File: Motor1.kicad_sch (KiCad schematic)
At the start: 53 parts, among them J601 Step Out, J604 Direction, J605 Direction, Q601 WSF07N10, Q602 WSF07N10, Q603 WSF07N10, Q604 WSF07N10, Q605 WSF07N10, Q606 WSF07N10, Q607 WSF07N10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

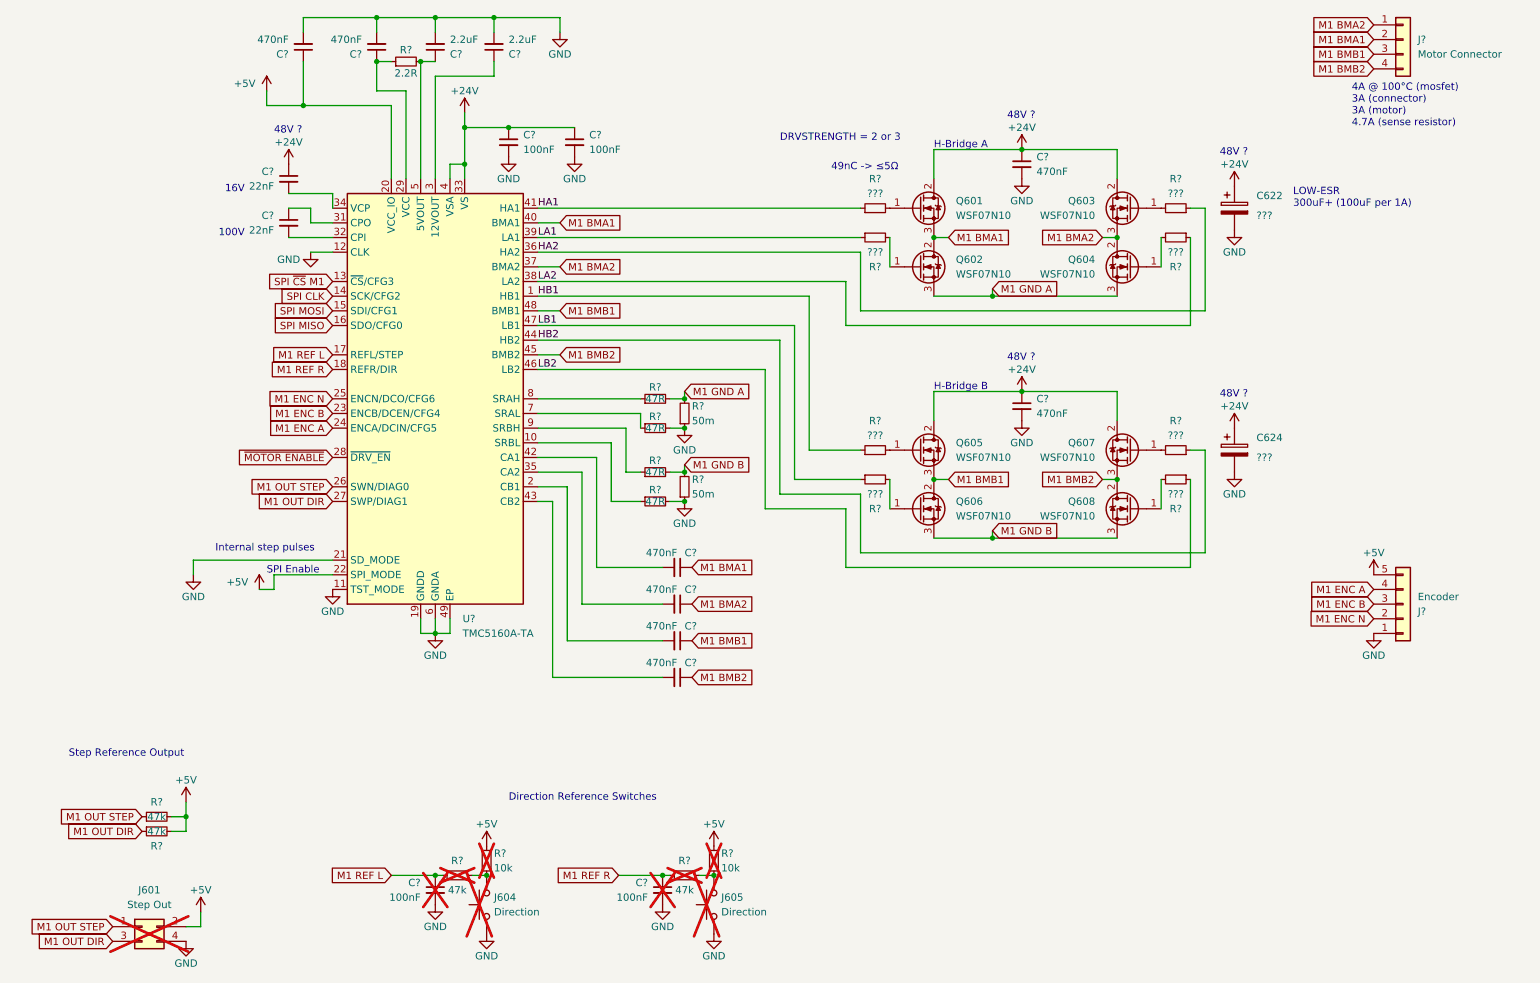
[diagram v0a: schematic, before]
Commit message: Complete schematics Assign every value (very few exceptions) Change TCM5160 from on-board to separate module Add fuses Add power supplies (LDO + 2x buck converter)
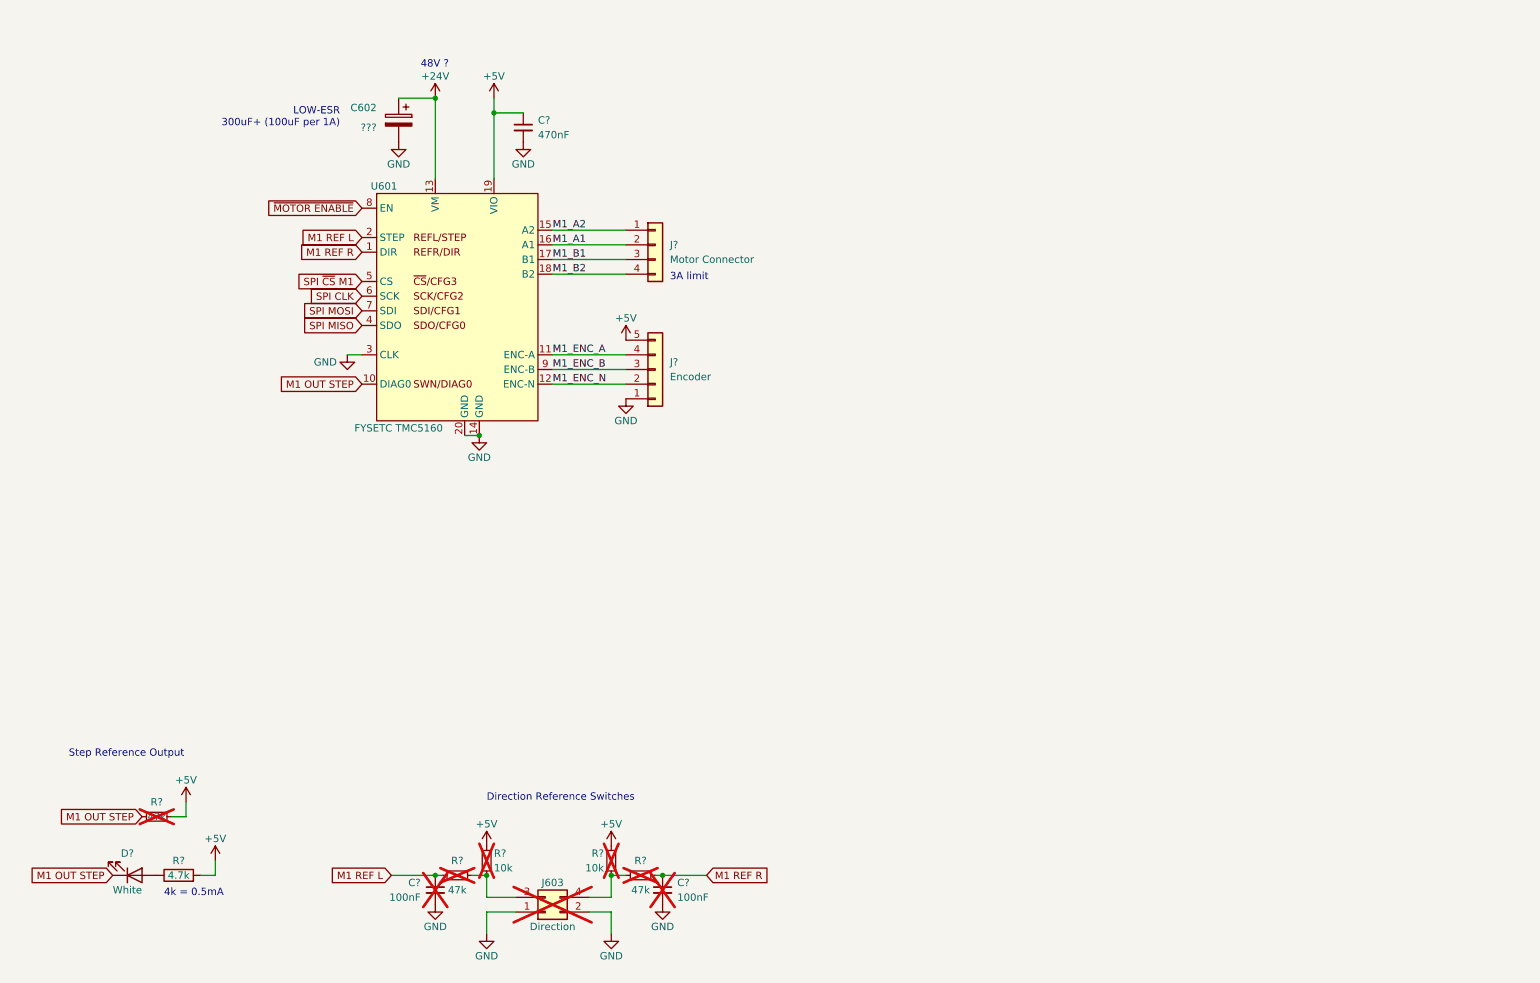
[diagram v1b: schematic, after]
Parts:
- removed C622, C624: ???, symbol Device:C_Polarized
- removed C? (x6): 470nF, Capacitor_SMD:C_1210_3225Metric, symbol Device:C_Small
- removed C? (x4): 100nF, symbol Device:C_Small
- removed C? (x2): 2.2uF, symbol Device:C_Small
- removed C? (x2): 470nF, symbol Device:C_Small
- removed C? (x2): 22nF, symbol Device:C_Small
- removed J601: Step Out, Connector_PinHeader_2.54mm:PinHeader_2x02_P2.54mm_Vertical, symbol Connector_Generic:Conn_02x02_Odd_Even
- removed J604, J605: Direction, Connector_PinHeader_2.54mm:PinHeader_1x02_P2.54mm_Vertical, symbol Switch:SW_Push
- removed J?: Encoder, Connector_JST:JST_XH_B5B-XH-A_1x05_P2.50mm_Vertical, symbol Connector_Generic:Conn_01x05
- removed J?: Motor Connector, Connector_JST:JST_XH_B4B-XH-A_1x04_P2.50mm_Vertical, symbol Connector_Generic:Conn_01x04
- removed Q601, Q602, Q603, Q604, Q605, Q606, Q607, Q608: WSF07N10, Package_TO_SOT_SMD:TO-252-2, symbol Transistor_FET:QM6006D
- removed R? (x2): 50m, Resistor_SMD:R_2512_6332Metric, symbol Device:R_Small
- removed R? (x4): 47k, symbol Device:R_Small
- removed R? (x8): ???, symbol Device:R_Small
- removed R? (x4): 47R, symbol Device:R_Small
- removed R?: 2.2R, symbol Device:R_Small
- removed R? (x2): 10k, symbol Device:R_Small
- removed U?: TMC5160A-TA, Package_QFP:TQFP-48-1EP_7x7mm_P0.5mm_EP5x5mm_ThermalVias, symbol Driver_Motor:TMC5160A-TA
- added C602: ???, symbol Device:C_Polarized
- added C? (x2): 100nF, Capacitor_SMD:C_0402_1005Metric, symbol Device:C_Small
- added C?: 470nF, Capacitor_SMD:C_0603_1608Metric, symbol Device:C_Small
- added D?: White, LED_SMD:LED_0402_1005Metric, symbol Device:LED
- added J603: Direction, Connector_PinHeader_2.54mm:PinHeader_2x02_P2.54mm_Vertical, symbol Connector_Generic:Conn_02x02_Odd_Even
- added J?: Motor Connector, Connector_JST:JST_XH_B4B-XH-A_1x04_P2.50mm_Vertical, symbol Connector_Generic:Conn_01x04
- added J?: Encoder, Connector_JST:JST_XH_B5B-XH-A_1x05_P2.50mm_Vertical, symbol Connector_Generic:Conn_01x05
- added R? (x3): 47k, Resistor_SMD:R_0603_1608Metric, symbol Device:R_Small
- added R? (x2): 10k, Resistor_SMD:R_0603_1608Metric, symbol Device:R_Small
- added R?: 4.7k, Resistor_SMD:R_0603_1608Metric, symbol Device:R
- added U601: FYSETC TMC5160, Custom:FYSETC TMC5160, symbol Custom:FYSETC_TMC5160
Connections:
- net +24V: now also C602.1, U601.13 (VM)
- net +5V: now also C?.1, J?.5 (Pin_5), R?.2, R?.2, R?.2, R?.2, U601.19 (VIO)
- net GND: now also C602.2, C?.2, C?.2, C?.2, J603.1 (Pin_1), J603.2 (Pin_2), J?.1 (Pin_1), U601.14 (GND), U601.20 (GND), U601.3 (CLK)
- net M1 OUT STEP: now also D?.1 (K), R?.1, U601.10 (DIAG0)
- net M1 REF L: now also C?.1, R?.1, U601.2 (STEP)
- net M1 REF R: now also C?.1, R?.1, U601.1 (DIR)
- net SPI CLK: now also U601.6 (SCK)
- net SPI MISO: now also U601.4 (SDO)
- net SPI MOSI: now also U601.7 (SDI)
- net SPI ~{CS} M1: now also U601.5 (CS)
- net ~{MOTOR ENABLE}: now also U601.8 (EN)
- new net: J603.3 (Pin_3), R?.1, R?.2
- new net: J603.4 (Pin_4), R?.1, R?.2
- new net: D?.2 (A), R?.1
- new net M1_A1: J?.2 (Pin_2), U601.16 (A1)
- new net M1_A2: J?.1 (Pin_1), U601.15 (A2)
- new net M1_B1: J?.3 (Pin_3), U601.17 (B1)
- new net M1_B2: J?.4 (Pin_4), U601.18 (B2)
- new net M1_ENC_A: J?.4 (Pin_4), U601.11 (ENC-A)
- new net M1_ENC_B: J?.3 (Pin_3), U601.9 (ENC-B)
- new net M1_ENC_N: J?.2 (Pin_2), U601.12 (ENC-N)
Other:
- note added: "3A limit"
- note added: "4k = 0.5mA"
- note removed: "100V"
- note removed: "16V"
- note removed: "49nC -> ≤5Ω"
- note removed: "4A @ 100°C (mosfet) 3A (connector) 3A (motor) 4.7A (sense resistor)"
- note removed: "DRVSTRENGTH = 2 or 3"
- note removed: "H-Bridge A"
- note removed: "H-Bridge B"
- note removed: "Internal step pulses"
- note removed: "SPI Enable"

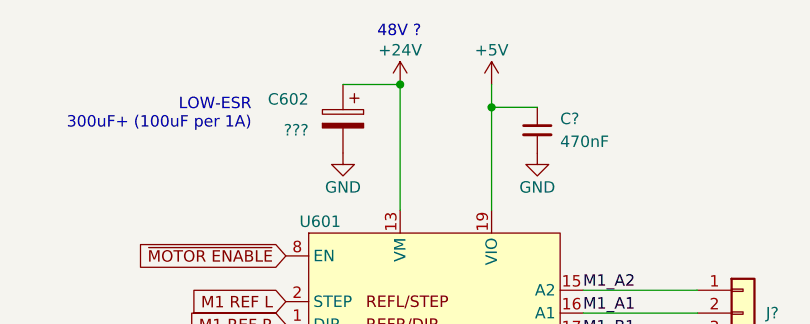
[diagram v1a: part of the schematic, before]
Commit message: More PCB placement, fix 48V for Motors
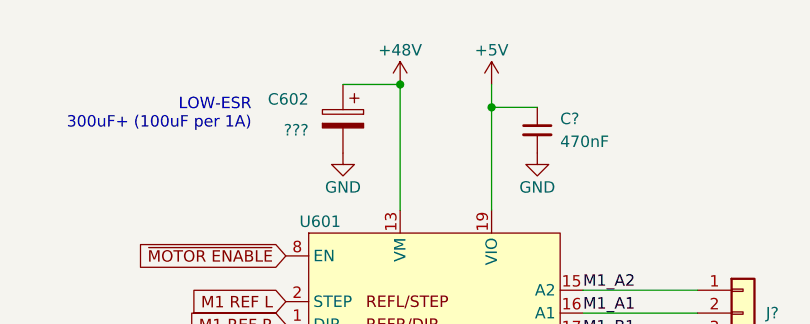
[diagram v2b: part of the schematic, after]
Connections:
- net +24V renamed +48V
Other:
- note removed: "48V ?"
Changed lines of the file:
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@@
   (junction (at 121.92 173.99) (diameter 0) (color 0 0 0 0)
   )
+  (junction (at 91.44 39.37) (diameter 0) (color 0 0 0 0)
+  )
   (junction (at 130.81 173.99) (diameter 0) (color 0 0 0 0)
   )
@@
   (junction (at 101.6 41.91) (diameter 0) (color 0 0 0 0)
   )
-  (junction (at 91.44 39.37) (diameter 0) (color 0 0 0 0)
-  )
   (wire (pts (xy 118.11 180.34) (xy 121.92 180.34))
     (stroke (width 0) (type default))
@@
   (wire (pts (xy 53.34 173.99) (xy 50.8 173.99))
     (stroke (width 0) (type default))
-  )
-  (text "48V ?" (at 88.9 34.29 0)
-    (effects (font (size 1.27 1.27)) (justify left bottom))
   )
   (text "Step Reference Output" (at 27.94 153.67 0)
@@
     )
   )
+  (symbol (lib_id "power:+48V") (at 91.44 39.37 0) (unit 1)
+    (in_bom yes) (on_board yes) (dnp no)
+    (property "Reference" "#PWR0204" (at 91.44 43.18 0)
+      (effects (font (size 1.27 1.27)) hide)
+    )
+    (property "Value" "+48V" (at 91.44 35.56 0)
+      (effects (font (size 1.27 1.27)))
+    )
+    (property "Footprint" "" (at 91.44 39.37 0)
+      (effects (font (size 1.27 1.27)) hide)
+    )
+    (property "Datasheet" "" (at 91.44 39.37 0)
+      (effects (font (size 1.27 1.27)) hide)
+    )
+    (pin "1")
+    (instances
+      (project "Can3DPrinter4Motor"
+        (path "/cb4e159a-5c17-494a-ba7f-10e700f814f1/e05e1111-b676-4692-8151-4de155805267"
+          (reference "#PWR0204") (unit 1)
+        )
+        (path "/cb4e159a-5c17-494a-ba7f-10e700f814f1"
+          (reference "#PWR0113") (unit 1)
+        )
+        (path "/cb4e159a-5c17-494a-ba7f-10e700f814f1/03ab3e80-f454-40c8-8f97-43a0b791de0b/a3514610-4e2d-47ba-84b8-39806e951746"
+          (reference "#PWR0602") (unit 1)
+        )
+      )
+    )
+  )
   (symbol (lib_id "Device:C_Small") (at 130.81 176.53 0) (unit 1)
     (in_bom yes) (on_board yes) (dnp yes)
@@
         )
       )
-    )
-  )
-  (symbol (lib_id "power:+24V") (at 91.44 39.37 0) (unit 1)
-    (in_bom yes) (on_board yes) (dnp no)
-    (property "Reference" "#PWR?" (at 91.44 43.18 0)
-      (effects (font (size 1.27 1.27)) hide)
-    )
-    (property "Value" "+24V" (at 91.44 35.56 0)
-      (effects (font (size 1.27 1.27)))
-    )
-    (property "Footprint" "" (at 91.44 39.37 0)
-      (effects (font (size 1.27 1.27)) hide)
-    )
-    (property "Datasheet" "" (at 91.44 39.37 0)
-      (effects (font (size 1.27 1.27)) hide)
-    )
-    (pin "1")
-    (instances
-      (project "Can3DPrinter4Motor"
-        (path "/cb4e159a-5c17-494a-ba7f-10e700f814f1/03ab3e80-f454-40c8-8f97-43a0b791de0b"
-          (reference "#PWR?") (unit 1)
-        )
-        (path "/cb4e159a-5c17-494a-ba7f-10e700f814f1/03ab3e80-f454-40c8-8f97-43a0b791de0b/a3514610-4e2d-47ba-84b8-39806e951746"
-          (reference "#PWR0635") (unit 1)
-        )
-        (path "/cb4e159a-5c17-494a-ba7f-10e700f814f1/03ab3e80-f454-40c8-8f97-43a0b791de0b/c731393f-82c9-42eb-b1cc-cc38a32cf9d8"
-          (reference "#PWR0705") (unit 1)
-        )
-        (path "/cb4e159a-5c17-494a-ba7f-10e700f814f1/03ab3e80-f454-40c8-8f97-43a0b791de0b/596394bf-80ea-4be7-ad96-94dd67657b85"
-          (reference "#PWR0805") (unit 1)
-        )
-        (path "/cb4e159a-5c17-494a-ba7f-10e700f814f1/03ab3e80-f454-40c8-8f97-43a0b791de0b/47aa3abf-8d06-4c45-872c-33ec1f9a6564"
-          (reference "#PWR0905") (unit 1)
-        )
-      )

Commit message: Finish wiring PCB
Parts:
- C602: footprint (none) -> Capacitor_THT:CP_Radial_D6.3mm_P2.50mm
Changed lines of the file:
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@@
     (pin "2")
     (instances
-      (project "Can3DPrinter4Motor"
+      (project "4MotorCAN"
         (path "/cb4e159a-5c17-494a-ba7f-10e700f814f1/03ab3e80-f454-40c8-8f97-43a0b791de0b"
           (reference "R?") (unit 1)
@@
     (pin "1")
     (instances
-      (project "Can3DPrinter4Motor"
+      (project "4MotorCAN"
         (path "/cb4e159a-5c17-494a-ba7f-10e700f814f1/03ab3e80-f454-40c8-8f97-43a0b791de0b"
           (reference "#PWR?") (unit 1)
@@
     (pin "1")
     (instances
-      (project "Can3DPrinter4Motor"
+      (project "4MotorCAN"
         (path "/cb4e159a-5c17-494a-ba7f-10e700f814f1/03ab3e80-f454-40c8-8f97-43a0b791de0b/a3514610-4e2d-47ba-84b8-39806e951746"
           (reference "#PWR0601") (unit 1)
@@
     (pin "1")
     (instances
-      (project "Can3DPrinter4Motor"
+      (project "4MotorCAN"
         (path "/cb4e159a-5c17-494a-ba7f-10e700f814f1/03ab3e80-f454-40c8-8f97-43a0b791de0b/a3514610-4e2d-47ba-84b8-39806e951746"
           (reference "#PWR0626") (unit 1)
@@
     (pin "1")
     (instances
-      (project "Can3DPrinter4Motor"
+      (project "4MotorCAN"
         (path "/cb4e159a-5c17-494a-ba7f-10e700f814f1/03ab3e80-f454-40c8-8f97-43a0b791de0b/a3514610-4e2d-47ba-84b8-39806e951746"
           (reference "#PWR0619") (unit 1)
@@
     (pin "2")
     (instances
-      (project "Can3DPrinter4Motor"
+      (project "4MotorCAN"
         (path "/cb4e159a-5c17-494a-ba7f-10e700f814f1/03ab3e80-f454-40c8-8f97-43a0b791de0b"
           (reference "C?") (unit 1)
@@
     (pin "1")
     (instances
-      (project "Can3DPrinter4Motor"
+      (project "4MotorCAN"
         (path "/cb4e159a-5c17-494a-ba7f-10e700f814f1/03ab3e80-f454-40c8-8f97-43a0b791de0b"
           (reference "#PWR?") (unit 1)
@@
     (pin "9")
     (instances
-      (project "Can3DPrinter4Motor"
+      (project "4MotorCAN"
         (path "/cb4e159a-5c17-494a-ba7f-10e700f814f1/03ab3e80-f454-40c8-8f97-43a0b791de0b/a3514610-4e2d-47ba-84b8-39806e951746"
           (reference "U601") (unit 1)
@@
     (pin "2")
     (instances
-      (project "Can3DPrinter4Motor"
+      (project "4MotorCAN"
         (path "/cb4e159a-5c17-494a-ba7f-10e700f814f1/03ab3e80-f454-40c8-8f97-43a0b791de0b"
           (reference "R?") (unit 1)
@@
     (pin "1")
     (instances
-      (project "Can3DPrinter4Motor"
+      (project "4MotorCAN"
         (path "/cb4e159a-5c17-494a-ba7f-10e700f814f1/03ab3e80-f454-40c8-8f97-43a0b791de0b"
           (reference "#PWR?") (unit 1)
@@
     (pin "4")
     (instances
-      (project "Can3DPrinter4Motor"
+      (project "4MotorCAN"
         (path "/cb4e159a-5c17-494a-ba7f-10e700f814f1/03ab3e80-f454-40c8-8f97-43a0b791de0b"
           (reference "J?") (unit 1)
@@
     (pin "5")
     (instances
-      (project "Can3DPrinter4Motor"
+      (project "4MotorCAN"
         (path "/cb4e159a-5c17-494a-ba7f-10e700f814f1/03ab3e80-f454-40c8-8f97-43a0b791de0b"
           (reference "J?") (unit 1)
@@
       (effects (font (size 1.27 1.27)) (justify left))
     )
-    (property "Footprint" "" (at 84.1248 46.99 0)
+    (property "Footprint" "Capacitor_THT:CP_Radial_D6.3mm_P2.50mm" (at 84.1248 46.99 0)
       (effects (font (size 1.27 1.27)) hide)
     )
@@
       (effects (font (size 1.27 1.27)) hide)
     )
-    (pin "1")
-    (pin "2")
-    (instances
-      (project "Can3DPrinter4Motor"
+    (property "LCSC" "" (at 85.09 43.18 0)
+      (effects (font (size 1.27 1.27)) hide)
+    )
+    (pin "1")
+    (pin "2")
+    (instances
+      (project "4MotorCAN"
         (path "/cb4e159a-5c17-494a-ba7f-10e700f814f1/03ab3e80-f454-40c8-8f97-43a0b791de0b/a3514610-4e2d-47ba-84b8-39806e951746"
           (reference "C602") (unit 1)
@@
     (pin "1")
     (instances
-      (project "Can3DPrinter4Motor"
+      (project "4MotorCAN"
         (path "/cb4e159a-5c17-494a-ba7f-10e700f814f1/03ab3e80-f454-40c8-8f97-43a0b791de0b"
           (reference "#PWR?") (unit 1)
@@
     (pin "1")
     (instances
-      (project "Can3DPrinter4Motor"
+      (project "4MotorCAN"
         (path "/cb4e159a-5c17-494a-ba7f-10e700f814f1/03ab3e80-f454-40c8-8f97-43a0b791de0b/a3514610-4e2d-47ba-84b8-39806e951746"
           (reference "#PWR0623") (unit 1)
@@
     (pin "1")
     (instances
-      (project "Can3DPrinter4Motor"
+      (project "4MotorCAN"
         (path "/cb4e159a-5c17-494a-ba7f-10e700f814f1/03ab3e80-f454-40c8-8f97-43a0b791de0b/a3514610-4e2d-47ba-84b8-39806e951746"
           (reference "#PWR0618") (unit 1)
@@
     (pin "1")
     (instances
-      (project "Can3DPrinter4Motor"
+      (project "4MotorCAN"
         (path "/cb4e159a-5c17-494a-ba7f-10e700f814f1/03ab3e80-f454-40c8-8f97-43a0b791de0b"
           (reference "#PWR?") (unit 1)
@@
     (pin "1")
     (instances
-      (project "Can3DPrinter4Motor"
+      (project "4MotorCAN"
         (path "/cb4e159a-5c17-494a-ba7f-10e700f814f1/03ab3e80-f454-40c8-8f97-43a0b791de0b/a3514610-4e2d-47ba-84b8-39806e951746"
           (reference "#PWR0634") (unit 1)
@@
     (pin "1")
     (instances
-      (project "Can3DPrinter4Motor"
+      (project "4MotorCAN"
         (path "/cb4e159a-5c17-494a-ba7f-10e700f814f1/03ab3e80-f454-40c8-8f97-43a0b791de0b"
           (reference "#PWR?") (unit 1)
@@
     (pin "1")
     (instances
-      (project "Can3DPrinter4Motor"
+      (project "4MotorCAN"
         (path "/cb4e159a-5c17-494a-ba7f-10e700f814f1/03ab3e80-f454-40c8-8f97-43a0b791de0b"
           (reference "#PWR?") (unit 1)
@@
     (pin "1")
     (instances
-      (project "Can3DPrinter4Motor"
+      (project "4MotorCAN"
         (path "/cb4e159a-5c17-494a-ba7f-10e700f814f1/e05e1111-b676-4692-8151-4de155805267"
           (reference "#PWR0204") (unit 1)
@@
     (pin "2")
     (instances
-      (project "Can3DPrinter4Motor"
+      (project "4MotorCAN"
         (path "/cb4e159a-5c17-494a-ba7f-10e700f814f1/03ab3e80-f454-40c8-8f97-43a0b791de0b"
           (reference "C?") (unit 1)
@@
     (pin "2")
     (instances
-      (project "Can3DPrinter4Motor"
+      (project "4MotorCAN"
         (path "/cb4e159a-5c17-494a-ba7f-10e700f814f1/03ab3e80-f454-40c8-8f97-43a0b791de0b"
           (reference "R?") (unit 1)
@@
     (pin "4")
     (instances
-      (project "Can3DPrinter4Motor"
+      (project "4MotorCAN"
         (path "/cb4e159a-5c17-494a-ba7f-10e700f814f1/03ab3e80-f454-40c8-8f97-43a0b791de0b/a3514610-4e2d-47ba-84b8-39806e951746"
           (reference "J603") (unit 1)
@@
     (pin "1")
     (instances
-      (project "Can3DPrinter4Motor"
+      (project "4MotorCAN"
         (path "/cb4e159a-5c17-494a-ba7f-10e700f814f1/03ab3e80-f454-40c8-8f97-43a0b791de0b"
           (reference "#PWR?") (unit 1)
@@
     (pin "2")
     (instances
-      (project "Can3DPrinter4Motor"
+      (project "4MotorCAN"
         (path "/cb4e159a-5c17-494a-ba7f-10e700f814f1/03ab3e80-f454-40c8-8f97-43a0b791de0b"
           (reference "C?") (unit 1)
@@
         )
       )
-      (project "Can3DPrinter4Motor"
+      (project "4MotorCAN"
         (path "/cb4e159a-5c17-494a-ba7f-10e700f814f1"
           (reference "D104") (unit 1)
@@
     (pin "2")
     (instances
-      (project "Can3DPrinter4Motor"
+      (project "4MotorCAN"
         (path "/cb4e159a-5c17-494a-ba7f-10e700f814f1/03ab3e80-f454-40c8-8f97-43a0b791de0b"
           (reference "R?") (unit 1)
@@
     (pin "2")
     (instances
-      (project "Can3DPrinter4Motor"
+      (project "4MotorCAN"
         (path "/cb4e159a-5c17-494a-ba7f-10e700f814f1/03ab3e80-f454-40c8-8f97-43a0b791de0b"
           (reference "R?") (unit 1)
@@
         )
       )
-      (project "Can3DPrinter4Motor"
+      (project "4MotorCAN"
         (path "/cb4e159a-5c17-494a-ba7f-10e700f814f1"
           (reference "R104") (unit 1)
@@
     (pin "1")
     (instances
-      (project "Can3DPrinter4Motor"
+      (project "4MotorCAN"
         (path "/cb4e159a-5c17-494a-ba7f-10e700f814f1/03ab3e80-f454-40c8-8f97-43a0b791de0b"
           (reference "#PWR?") (unit 1)
